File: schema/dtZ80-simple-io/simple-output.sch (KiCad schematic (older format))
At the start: 14 parts, among them J1 Conn_01x40, U1 74LS138, U2 74LS573, U3 74LS573, U4 74HC00, U5 HDSP-A151, U6 HDSP-A151

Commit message: Reworked Boards
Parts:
- removed C?: C, symbol Device:C
- removed J1: Conn_01x40, Connector_PinSocket_2.54mm:PinSocket_1x40_P2.54mm_Horizontal, symbol Connector_Generic:Conn_01x40
- removed U3: 74LS573, Package_DIP:DIP-20_W7.62mm_Socket, symbol 74xx:74LS573
- removed U4: 74HC00, Package_DIP:DIP-14_W10.16mm, symbol 74xx:74HC00
- removed U5, U6: HDSP-A151, Display_7Segment:HDSP-A151, symbol Display_Character:HDSP-A151
- removed U?: NE555P, Package_DIP:DIP-8_W7.62mm, symbol Timer:NE555P
- added C1, C4, C5: 100n, Capacitor_THT:C_Disc_D4.3mm_W1.9mm_P5.00mm, symbol Device:C
- added C3, C6: 22pF, Capacitor_THT:C_Disc_D4.3mm_W1.9mm_P5.00mm, symbol Device:C
- added IC1: Z80SIO, Package_DIP:DIP-40_W15.24mm_Socket, symbol Z80SIO:Z80SIO
- added IC2: Z80CTC, Package_DIP:DIP-28_W15.24mm_Socket, symbol Z80CTC:Z80CTC
- added J1: RC2014Bus, Connector_PinHeader_2.54mm:PinHeader_1x40_P2.54mm_Vertical, symbol rc2014bus:RC2014Bus
- added J2: 8 Bit Port, Connector_PinHeader_2.54mm:PinHeader_2x07_P2.54mm_Vertical, symbol Connector_Generic:Conn_02x07_Top_Bottom
- added J3: FT_232, Connector_PinHeader_2.54mm:PinHeader_1x06_P2.54mm_Vertical, symbol Connector_Generic:Conn_01x06
- added J4: Mini-DIN-6, package_connectors:Mini_DIN_6_TE_Connectivity, symbol Connector:Mini-DIN-6
- added Jumper1: Conn_01x02, Connector_PinHeader_2.54mm:PinHeader_1x02_P2.54mm_Vertical, symbol Connector_Generic:Conn_01x02
- added Q1, Q2: Q_NPN_BCE, Package_TO_SOT_THT:TO-92_HandSolder, symbol Device:Q_NPN_BCE
- added R10: 1k, Resistor_THT:R_Axial_DIN0204_L3.6mm_D1.6mm_P5.08mm_Horizontal, symbol Device:R
- added R11, R12, R13, R14: 5K, Resistor_THT:R_Axial_DIN0204_L3.6mm_D1.6mm_P5.08mm_Horizontal, symbol Device:R
- added R5, R7: 10K, Resistor_THT:R_Axial_DIN0204_L3.6mm_D1.6mm_P5.08mm_Horizontal, symbol Device:R
- added R6, R8, R9: 2K, Resistor_THT:R_Axial_DIN0204_L3.6mm_D1.6mm_P5.08mm_Horizontal, symbol Device:R
- added U1: 74LS04, Package_DIP:DIP-14_W7.62mm_Socket, symbol 74xx:74LS04
- added U4, U8: 74HC245, Package_DIP:DIP-20_W7.62mm_Socket, symbol 74xx:74HC245
- added U5: 5161AS, 7seg:7SegmentLED_LTS6760_LTS6780, symbol 7seg:5161AS
- added Y1: Crystal, Crystal:Crystal_HC49-U_Vertical, symbol Device:Crystal
- C2: renamed from C1; value 10u -> 100n; footprint Capacitor_THT:CP_Radial_Tantal_D4.5mm_P5.00mm -> Capacitor_THT:C_Disc_D4.3mm_W1.9mm_P5.00mm
- R1: footprint Resistor_THT:R_Axial_DIN0204_L3.6mm_D1.6mm_P1.90mm_Vertical -> Resistor_THT:R_Axial_DIN0204_L3.6mm_D1.6mm_P5.08mm_Horizontal
- R2: value 1k -> 220; footprint Resistor_THT:R_Axial_DIN0204_L3.6mm_D1.6mm_P1.90mm_Vertical -> Resistor_THT:R_Axial_DIN0204_L3.6mm_D1.6mm_P5.08mm_Horizontal
- R3: value 220 -> 1M; footprint Resistor_THT:R_Axial_DIN0204_L3.6mm_D1.6mm_P1.90mm_Vertical -> Resistor_THT:R_Axial_DIN0204_L3.6mm_D1.6mm_P5.08mm_Horizontal
- R4: value 220 -> 1K; footprint Resistor_THT:R_Axial_DIN0204_L3.6mm_D1.6mm_P1.90mm_Vertical -> Resistor_THT:R_Axial_DIN0204_L3.6mm_D1.6mm_P5.08mm_Horizontal
- renumbered U1 to U2, U2 to U3
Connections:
- net labels added: A4, CLK7.3728, D1, D2, D3, D4, D5, D6, IO0, IO1, IO2, IO3, IO4, IO5, IO6, IO7, KEY_CLK, KEY_DATA, RTS, RX, SIO_IEI, TX, UART_CLK, Y1, ~INT~, ~IORQ~, ~M1~, ~RD~, ~RESET~, ~WR~, ~Y0~, ~Y1~, ~Y2~, ~Y3~, ~Y4~
- net labels removed: A15, A8, IORQ, M1, WR
- wire segments 109 -> 233
- no-connect marks 33 -> 44
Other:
- note added: "CTS"
- note added: "DTR\n"
- note added: "GND"
- note added: "RX\n"
- note added: "TODO:\nWR in 138?"
- note added: "TX"
- note added: "VCC"
- note added: "Y0 = 7Seg\nY1 = 8 Bit In/Out\nY2 = Serial\nY3 = CTC\nY4 = PS/2"
- moved on the sheet: C2

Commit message: Schema
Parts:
- added J5: CTC, Connector_PinHeader_2.54mm:PinHeader_1x05_P2.54mm_Vertical, symbol Connector:Conn_01x05_Male
- J4: value Mini-DIN-6 -> PS/2 Keyboard
- Q1, Q2: value Q_NPN_BCE -> NPN
- renumbered Jumper1 to J1_5VtoSerial1
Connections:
- wire segments 233 -> 242
- no-connect marks 44 -> 39
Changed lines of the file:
@@
 	7450 1950 7450 1250
 $Comp
-L Connector_Generic:Conn_01x02 Jumper1
+L Connector_Generic:Conn_01x02 J1_5VtoSerial1
 U 1 1 6000661D
 P 7650 1150
-F 0 "Jumper1" H 7730 1142 50  0000 L CNN
+F 0 "J1_5VtoSerial1" H 7730 1142 50  0000 L CNN
 F 1 "Conn_01x02" H 7730 1051 50  0000 L CNN
 F 2 "Connector_PinHeader_2.54mm:PinHeader_1x02_P2.54mm_Vertical" H 7650 1150 50  0001 C CNN
@@
 P 7800 3500
 F 0 "J4" H 7800 3867 50  0000 C CNN
-F 1 "Mini-DIN-6" H 7800 3776 50  0000 C CNN
+F 1 "PS/2 Keyboard" H 7800 3776 50  0000 C CNN
 F 2 "package_connectors:Mini_DIN_6_TE_Connectivity" H 7800 3500 50  0001 C CNN
 F 3 "http://service.powerdynamics.com/ec/Catalog17/Section%2011.pdf" H 7800 3500 50  0001 C CNN
@@
 	1    0    0    -1
 $EndComp
-NoConn ~ 10750 1400
-NoConn ~ 10750 1500
-NoConn ~ 10750 1700
-NoConn ~ 10750 1800
-NoConn ~ 10750 2000
 Wire Wire Line
 	6600 2350 6800 2350
@@
 P 9950 4850
 F 0 "Q1" H 10141 4896 50  0000 L CNN
-F 1 "Q_NPN_BCE" H 10141 4805 50  0000 L CNN
+F 1 "NPN" H 10141 4805 50  0000 L CNN
 F 2 "Package_TO_SOT_THT:TO-92_HandSolder" H 10150 4950 50  0001 C CNN
 F 3 "~" H 9950 4850 50  0001 C CNN
@@
 P 9950 5350
 F 0 "Q2" H 10141 5396 50  0000 L CNN
-F 1 "Q_NPN_BCE" H 10141 5305 50  0000 L CNN
+F 1 "NPN" H 10141 5305 50  0000 L CNN
 F 2 "Package_TO_SOT_THT:TO-92_HandSolder" H 10150 5450 50  0001 C CNN
 F 3 "~" H 9950 5350 50  0001 C CNN
@@
 Wire Wire Line
 	9750 4850 9250 4850
+$Comp
+L Connector:Conn_01x05_Male J5
+U 1 1 6022B825
+P 11200 1600
+F 0 "J5" H 11172 1624 50  0000 R CNN
+F 1 "CTC" H 11172 1533 50  0000 R CNN
+F 2 "Connector_PinHeader_2.54mm:PinHeader_1x05_P2.54mm_Vertical" H 11200 1600 50  0001 C CNN
+F 3 "~" H 11200 1600 50  0001 C CNN
+	1    11200 1600
+	-1   0    0    -1
+$EndComp
+Wire Wire Line
+	10750 1400 11000 1400
+Wire Wire Line
+	10750 1500 11000 1500
+Wire Wire Line
+	10750 1700 10750 1600
+Wire Wire Line
+	10750 1600 11000 1600
+Wire Wire Line
+	10750 1800 10850 1800
+Wire Wire Line
+	10850 1800 10850 1700
+Wire Wire Line
+	10850 1700 11000 1700
+Wire Wire Line
+	10750 2000 11000 2000
+Wire Wire Line
+	11000 2000 11000 1800
 $EndSCHEMATC

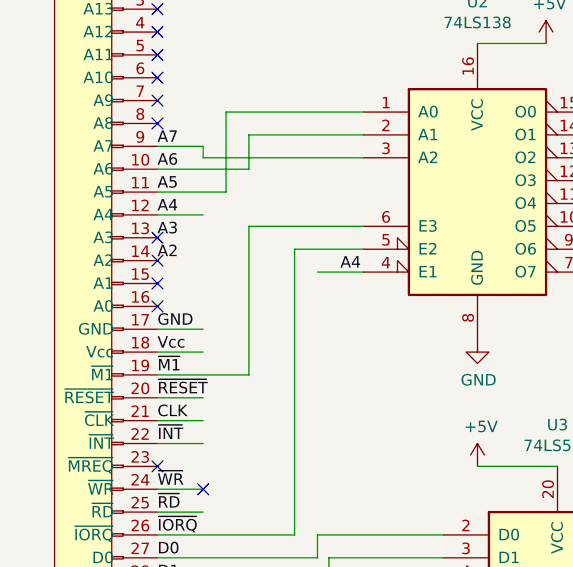
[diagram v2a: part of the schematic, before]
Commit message: CTC & Fixes on IO Board
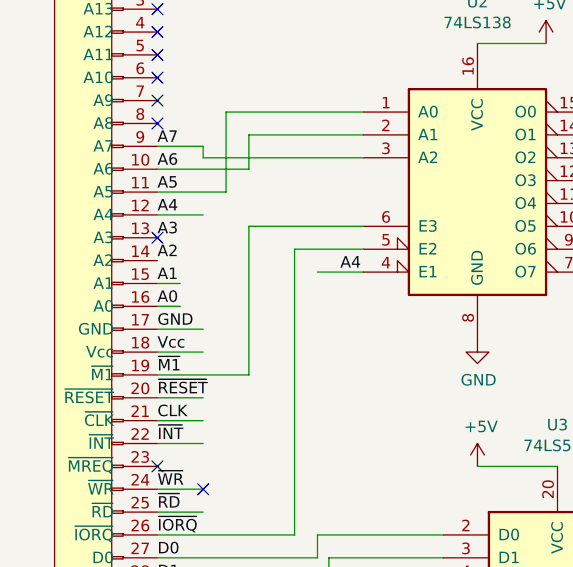
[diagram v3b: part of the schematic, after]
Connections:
- wire segments 242 -> 244
- no-connect marks 39 -> 36
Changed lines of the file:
@@
 Text Label 1250 2700 0    50   ~ 0
 A3
-Text Label 1250 2800 0    50   ~ 0
-A2
 Text Label 1250 3200 0    50   ~ 0
 Vcc
@@
 NoConn ~ 1250 4900
 NoConn ~ 1250 2700
-NoConn ~ 1250 2800
-NoConn ~ 1250 2900
-NoConn ~ 1250 3000
 NoConn ~ 1250 5200
 NoConn ~ 1250 5300
@@
 Wire Wire Line
 	11000 2000 11000 1800
+Wire Wire Line
+	1250 2900 1350 2900
+Wire Wire Line
+	1250 3000 1350 3000
+Text Label 1250 2900 0    50   ~ 0
+A1
+Text Label 1250 3000 0    50   ~ 0
+A0
+Text Label 1250 2800 0    50   ~ 0
+A2
 $EndSCHEMATC

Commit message: Cleanups, PDF-Exports
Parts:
- U5: symbol 7seg:5161AS -> simple-output-rescue:5161AS-7seg
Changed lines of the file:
@@
 ~Y2~
 $Comp
-L 7seg:5161AS U5
+L simple-output-rescue:5161AS-7seg U5
 U 1 1 603C9B68
 P 4100 4300
